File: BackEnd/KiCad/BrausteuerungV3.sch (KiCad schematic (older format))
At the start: 13 parts, among them IC1 DS18B20, J1 KHTaster, J2 myPiezzo, J3 Transmitter433MHz, J4 HC-06, P1 CONN_01X02, U1 arduino_nano

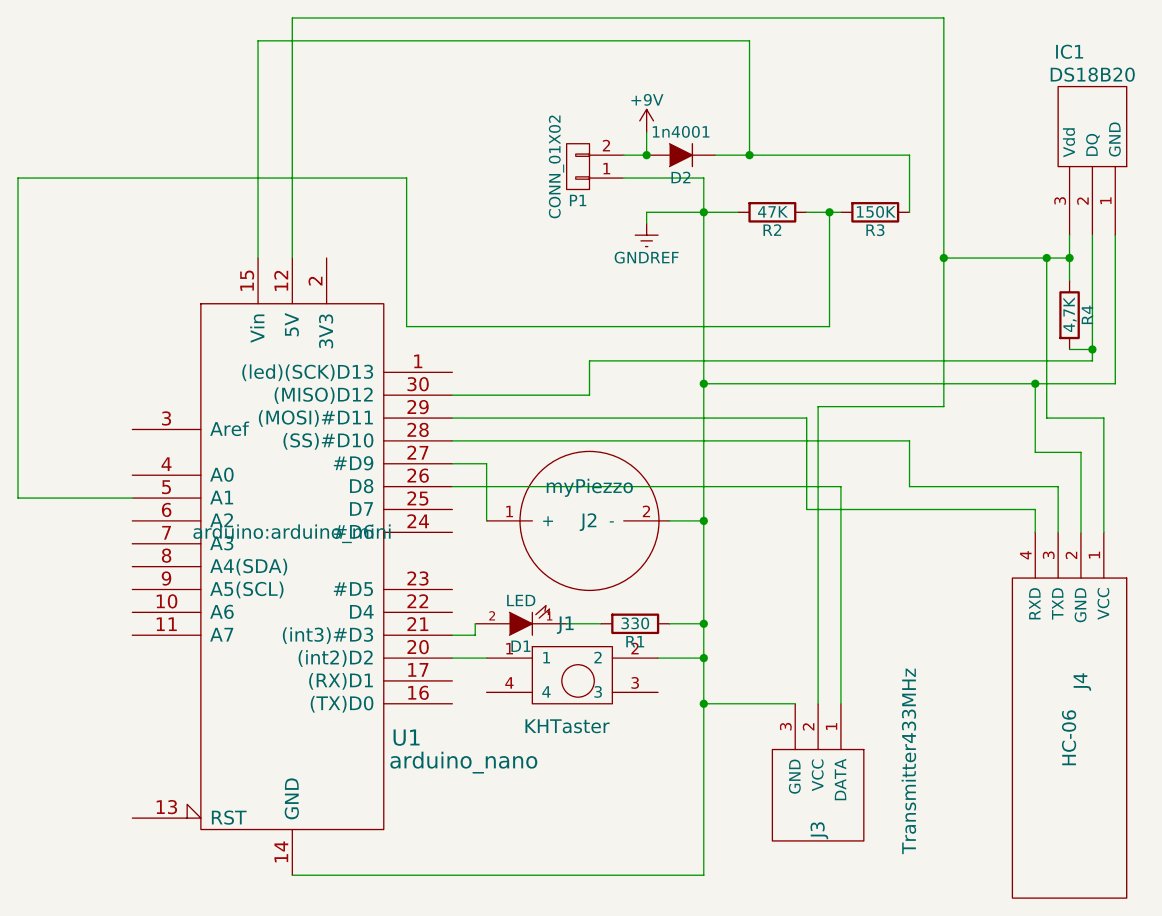
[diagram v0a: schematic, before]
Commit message: added voltage divider KiCad
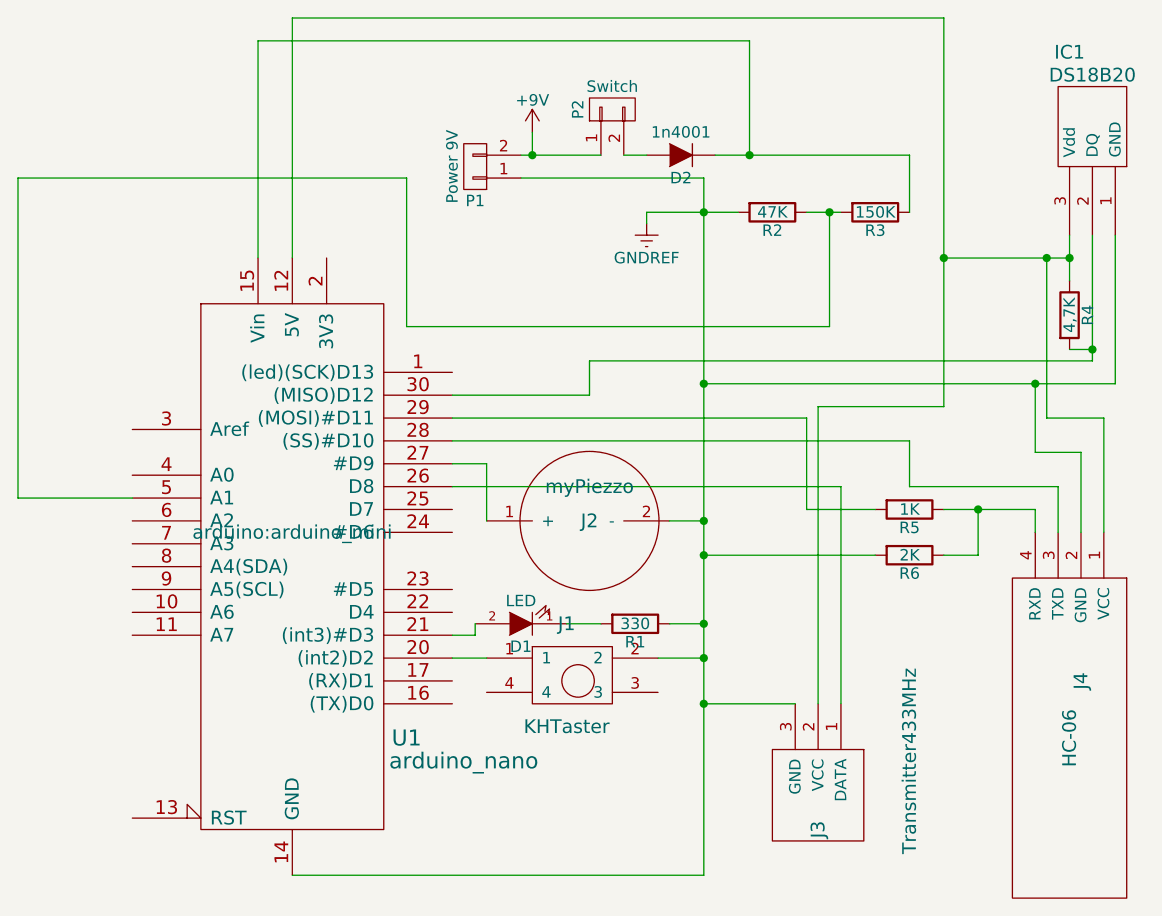
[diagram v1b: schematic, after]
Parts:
- added P2: Switch, LEDs:LED-3MM, symbol CONN_01X02
- added R5: 1K, symbol R
- added R6: 2K, symbol R
- P1: value CONN_01X02 -> Power 9V
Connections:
- net +9V: now also P2.1 (P1); no longer D2.2 (A)
- net GNDREF: now also R6.2
- net at U1.29 ((MOSI)#D11): now also R5.2; no longer J4.4 (RXD)
- new net: J4.4 (RXD), R5.1, R6.1
- new net: D2.2 (A), P2.2 (P2)
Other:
- moved on the sheet: P1
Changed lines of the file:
@@
 $EndComp
 $Comp
-L GNDREF #PWR01
+L GNDREF #PWR2
 U 1 1 5789029A
 P 6700 1650
-F 0 "#PWR01" H 6700 1400 50  0001 C CNN
+F 0 "#PWR2" H 6700 1400 50  0001 C CNN
 F 1 "GNDREF" H 6700 1500 50  0000 C CNN
 F 2 "" H 6700 1650 50  0000 C CNN
@@
 $EndComp
 $Comp
-L +9V #PWR02
+L +9V #PWR1
 U 1 1 5789049D
-P 6700 1250
-F 0 "#PWR02" H 6700 1100 50  0001 C CNN
-F 1 "+9V" H 6700 1390 50  0000 C CNN
-F 2 "" H 6700 1250 50  0000 C CNN
-F 3 "" H 6700 1250 50  0000 C CNN
-	1    6700 1250
+P 6200 1250
+F 0 "#PWR1" H 6200 1100 50  0001 C CNN
+F 1 "+9V" H 6200 1390 50  0000 C CNN
+F 2 "" H 6200 1250 50  0000 C CNN
+F 3 "" H 6200 1250 50  0000 C CNN
+	1    6200 1250
 	1    0    0    -1
 $EndComp
@@
 	7400 2500 7400 2900
 Wire Wire Line
-	7400 2900 8400 2900
-Wire Wire Line
 	8400 2900 8400 3000
 Wire Wire Line
@@
 L CONN_01X02 P1
 U 1 1 579E1182
-P 6400 1400
-F 0 "P1" H 6400 1550 50  0000 C CNN
-F 1 "CONN_01X02" V 6500 1400 50  0000 C CNN
-F 2 "LEDs:LED-3MM" H 6400 1400 50  0001 C CNN
-F 3 "" H 6400 1400 50  0000 C CNN
-	1    6400 1400
+P 5950 1400
+F 0 "P1" H 5950 1550 50  0000 C CNN
+F 1 "Power 9V" V 6050 1400 50  0000 C CNN
+F 2 "LEDs:LED-3MM" H 5950 1400 50  0001 C CNN
+F 3 "" H 5950 1400 50  0000 C CNN
+	1    5950 1400
 	-1   0    0    1
 $EndComp
 Wire Wire Line
-	6600 1450 6950 1450
+	6150 1450 6950 1450
 Wire Wire Line
 	6950 1450 6950 4500
@@
 	6600 1350 6700 1350
 Wire Wire Line
-	6700 1350 6700 1250
-Connection ~ 6700 1350
-Wire Wire Line
 	8650 2250 8650 1700
+$Comp
+L R R5
+U 1 1 5A568ECA
+P 7850 2900
+F 0 "R5" V 7930 2900 50  0000 C CNN
+F 1 "1K" V 7850 2900 50  0000 C CNN
+F 2 "" V 7780 2900 50  0000 C CNN
+F 3 "" H 7850 2900 50  0000 C CNN
+	1    7850 2900
+	0    1    1    0
+$EndComp
+Wire Wire Line
+	7400 2900 7700 2900
+Wire Wire Line
+	8000 2900 8400 2900
+$Comp
+L R R6
+U 1 1 5A5691D6
+P 7850 3100
+F 0 "R6" V 7930 3100 50  0000 C CNN
+F 1 "2K" V 7850 3100 50  0000 C CNN
+F 2 "" V 7780 3100 50  0000 C CNN
+F 3 "" H 7850 3100 50  0000 C CNN
+	1    7850 3100
+	0    1    1    0
+$EndComp
+Wire Wire Line
+	8000 3100 8150 3100
+Wire Wire Line
+	8150 3100 8150 2900
+Connection ~ 8150 2900
+Wire Wire Line
+	7700 3100 6950 3100
+Connection ~ 6950 3100
+Wire Wire Line
+	6150 1350 6500 1350
+Wire Wire Line
+	6200 1350 6200 1250
+$Comp
+L CONN_01X02 P2
+U 1 1 5A56A656
+P 6550 1150
+F 0 "P2" H 6550 1300 50  0000 C CNN
+F 1 "Switch" V 6650 1150 50  0000 C CNN
+F 2 "LEDs:LED-3MM" H 6550 1150 50  0001 C CNN
+F 3 "" H 6550 1150 50  0000 C CNN
+	1    6550 1150
+	0    -1   -1   0
+$EndComp
+Connection ~ 6200 1350
 $EndSCHEMATC

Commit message: added kicad layout
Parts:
- D1: footprint LEDs:LED-3MM -> Resistors_THT:R_Axial_DIN0204_L3.6mm_D1.6mm_P1.90mm_Vertical; symbol LED -> LED-RESCUE-BrausteuerungV3
- D2: footprint Resistors_ThroughHole:R_Axial_DIN0207_L6.3mm_D2.5mm_P7.62mm_Horizontal -> Resistors_THT:R_Axial_DIN0207_L6.3mm_D2.5mm_P10.16mm_Horizontal
- P1, P2: footprint LEDs:LED-3MM -> Resistors_THT:R_Axial_DIN0204_L3.6mm_D1.6mm_P1.90mm_Vertical
- R1, R2, R3, R4: footprint Resistors_ThroughHole:Resistor_Horizontal_RM10mm -> Resistors_THT:R_Axial_DIN0207_L6.3mm_D2.5mm_P10.16mm_Horizontal
- R5, R6: footprint (none) -> Resistors_THT:R_Axial_DIN0207_L6.3mm_D2.5mm_P10.16mm_Horizontal
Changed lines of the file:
@@
 EESchema Schematic File Version 2
+LIBS:BrausteuerungV3-rescue
 LIBS:myPiezzo
 LIBS:khtaster
 LIBS:hc-06
-LIBS:BrausteuerungV3-rescue
 LIBS:Transmitter433MHz
 LIBS:DS1820
@@
 F 0 "R4" V 8630 2050 50  0000 C CNN
 F 1 "4,7K" V 8550 2050 50  0000 C CNN
-F 2 "Resistors_ThroughHole:Resistor_Horizontal_RM10mm" V 8480 2050 50  0001 C CNN
+F 2 "Resistors_THT:R_Axial_DIN0207_L6.3mm_D2.5mm_P10.16mm_Horizontal" V 8480 2050 50  0001 C CNN
 F 3 "" H 8550 2050 50  0000 C CNN
 	1    8550 2050
@@
 F 0 "R1" V 6730 3400 50  0000 C CNN
 F 1 "330" V 6650 3400 50  0000 C CNN
-F 2 "Resistors_ThroughHole:Resistor_Horizontal_RM10mm" V 6580 3400 50  0001 C CNN
+F 2 "Resistors_THT:R_Axial_DIN0207_L6.3mm_D2.5mm_P10.16mm_Horizontal" V 6580 3400 50  0001 C CNN
 F 3 "" H 6650 3400 50  0000 C CNN
 	1    6650 3400
@@
 F 0 "R2" V 7330 1600 50  0000 C CNN
 F 1 "47K" V 7250 1600 50  0000 C CNN
-F 2 "Resistors_ThroughHole:Resistor_Horizontal_RM10mm" V 7180 1600 50  0001 C CNN
+F 2 "Resistors_THT:R_Axial_DIN0207_L6.3mm_D2.5mm_P10.16mm_Horizontal" V 7180 1600 50  0001 C CNN
 F 3 "" H 7250 1600 50  0000 C CNN
 	1    7250 1600
@@
 F 0 "R3" V 7780 1600 50  0000 C CNN
 F 1 "150K" V 7700 1600 50  0000 C CNN
-F 2 "Resistors_ThroughHole:Resistor_Horizontal_RM10mm" V 7630 1600 50  0001 C CNN
+F 2 "Resistors_THT:R_Axial_DIN0207_L6.3mm_D2.5mm_P10.16mm_Horizontal" V 7630 1600 50  0001 C CNN
 F 3 "" H 7700 1600 50  0000 C CNN
 	1    7700 1600
@@
 $EndComp
 $Comp
-L LED D1
+L LED-RESCUE-BrausteuerungV3 D1
 U 1 1 5788DA4B
 P 6150 3400
 F 0 "D1" H 6150 3500 50  0000 C CNN
 F 1 "LED" H 6150 3300 50  0000 C CNN
-F 2 "LEDs:LED-3MM" H 6150 3400 50  0001 C CNN
+F 2 "Resistors_THT:R_Axial_DIN0204_L3.6mm_D1.6mm_P1.90mm_Vertical" H 6150 3400 50  0001 C CNN
 F 3 "" H 6150 3400 50  0000 C CNN
 	1    6150 3400
@@
 $EndComp
 $Comp
-L GNDREF #PWR2
+L GNDREF #PWR01
 U 1 1 5789029A
 P 6700 1650
-F 0 "#PWR2" H 6700 1400 50  0001 C CNN
+F 0 "#PWR01" H 6700 1400 50  0001 C CNN
 F 1 "GNDREF" H 6700 1500 50  0000 C CNN
 F 2 "" H 6700 1650 50  0000 C CNN
@@
 $EndComp
 $Comp
-L +9V #PWR1
+L +9V #PWR02
 U 1 1 5789049D
 P 6200 1250
-F 0 "#PWR1" H 6200 1100 50  0001 C CNN
+F 0 "#PWR02" H 6200 1100 50  0001 C CNN
 F 1 "+9V" H 6200 1390 50  0000 C CNN
 F 2 "" H 6200 1250 50  0000 C CNN
@@
 F 0 "P1" H 5950 1550 50  0000 C CNN
 F 1 "Power 9V" V 6050 1400 50  0000 C CNN
-F 2 "LEDs:LED-3MM" H 5950 1400 50  0001 C CNN
+F 2 "Resistors_THT:R_Axial_DIN0204_L3.6mm_D1.6mm_P1.90mm_Vertical" H 5950 1400 50  0001 C CNN
 F 3 "" H 5950 1400 50  0000 C CNN
 	1    5950 1400
@@
 F 0 "D2" H 6850 1450 50  0000 C CNN
 F 1 "1n4001" H 6850 1250 50  0000 C CNN
-F 2 "Resistors_ThroughHole:R_Axial_DIN0207_L6.3mm_D2.5mm_P7.62mm_Horizontal" H 6850 1350 50  0001 C CNN
+F 2 "Resistors_THT:R_Axial_DIN0207_L6.3mm_D2.5mm_P10.16mm_Horizontal" H 6850 1350 50  0001 C CNN
 F 3 "" H 6850 1350 50  0000 C CNN
 	1    6850 1350
@@
 F 0 "R5" V 7930 2900 50  0000 C CNN
 F 1 "1K" V 7850 2900 50  0000 C CNN
-F 2 "" V 7780 2900 50  0000 C CNN
+F 2 "Resistors_THT:R_Axial_DIN0207_L6.3mm_D2.5mm_P10.16mm_Horizontal" V 7780 2900 50  0001 C CNN
 F 3 "" H 7850 2900 50  0000 C CNN
 	1    7850 2900
@@
 F 0 "R6" V 7930 3100 50  0000 C CNN
 F 1 "2K" V 7850 3100 50  0000 C CNN
-F 2 "" V 7780 3100 50  0000 C CNN
+F 2 "Resistors_THT:R_Axial_DIN0207_L6.3mm_D2.5mm_P10.16mm_Horizontal" V 7780 3100 50  0001 C CNN
 F 3 "" H 7850 3100 50  0000 C CNN
 	1    7850 3100
@@
 F 0 "P2" H 6550 1300 50  0000 C CNN
 F 1 "Switch" V 6650 1150 50  0000 C CNN
-F 2 "LEDs:LED-3MM" H 6550 1150 50  0001 C CNN
+F 2 "Resistors_THT:R_Axial_DIN0204_L3.6mm_D1.6mm_P1.90mm_Vertical" H 6550 1150 50  0001 C CNN
 F 3 "" H 6550 1150 50  0000 C CNN
 	1    6550 1150

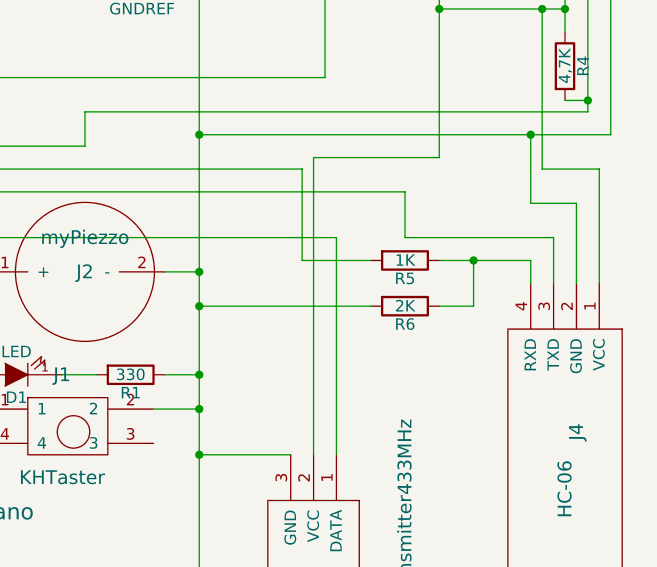
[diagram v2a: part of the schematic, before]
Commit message: spannunsgteiler andere widerstandswerte
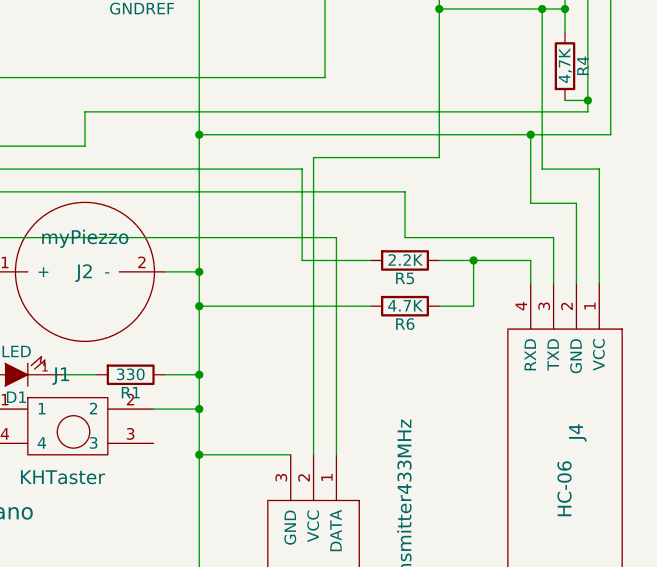
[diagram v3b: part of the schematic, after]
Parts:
- R5: value 1K -> 2.2K
- R6: value 2K -> 4.7K
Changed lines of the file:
@@
 P 7850 2900
 F 0 "R5" V 7930 2900 50  0000 C CNN
-F 1 "1K" V 7850 2900 50  0000 C CNN
+F 1 "2.2K" V 7850 2900 50  0000 C CNN
 F 2 "Resistors_THT:R_Axial_DIN0207_L6.3mm_D2.5mm_P10.16mm_Horizontal" V 7780 2900 50  0001 C CNN
 F 3 "" H 7850 2900 50  0000 C CNN
@@
 P 7850 3100
 F 0 "R6" V 7930 3100 50  0000 C CNN
-F 1 "2K" V 7850 3100 50  0000 C CNN
+F 1 "4.7K" V 7850 3100 50  0000 C CNN
 F 2 "Resistors_THT:R_Axial_DIN0207_L6.3mm_D2.5mm_P10.16mm_Horizontal" V 7780 3100 50  0001 C CNN
 F 3 "" H 7850 3100 50  0000 C CNN
